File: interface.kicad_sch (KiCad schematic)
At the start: 12 parts, among them IC107 RC4558, IC501 D91317GD, IC502 MSM5205, IC503 4053, IC504 4053

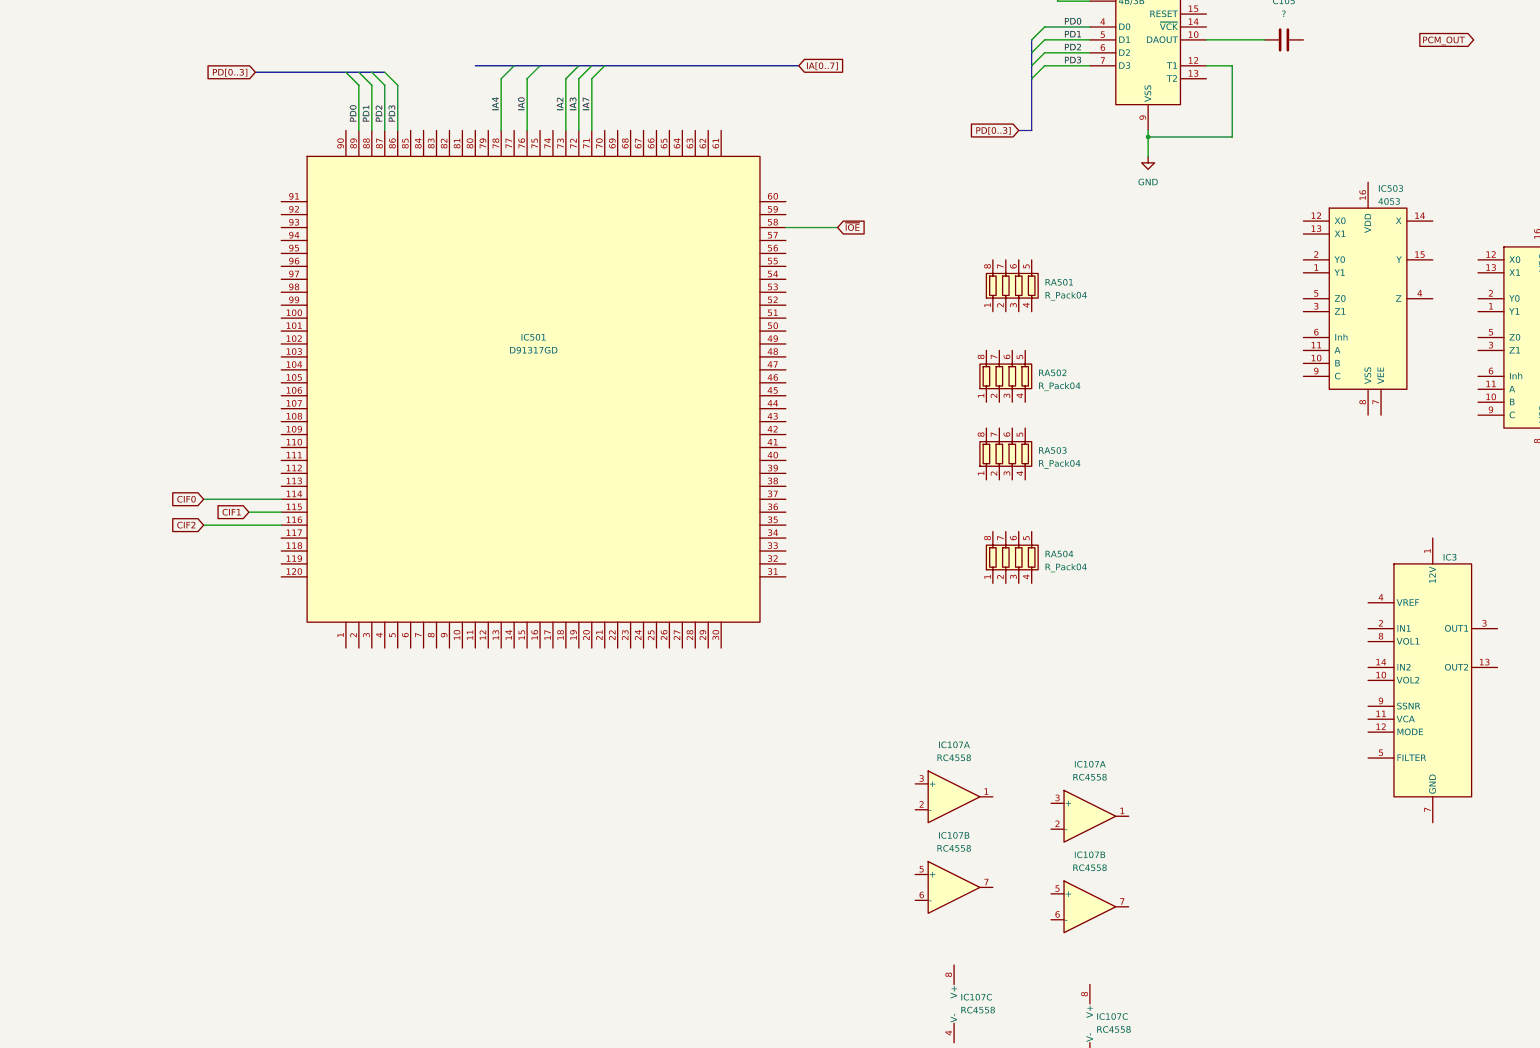
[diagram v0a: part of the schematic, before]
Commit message: Add proper scans, redo traces.
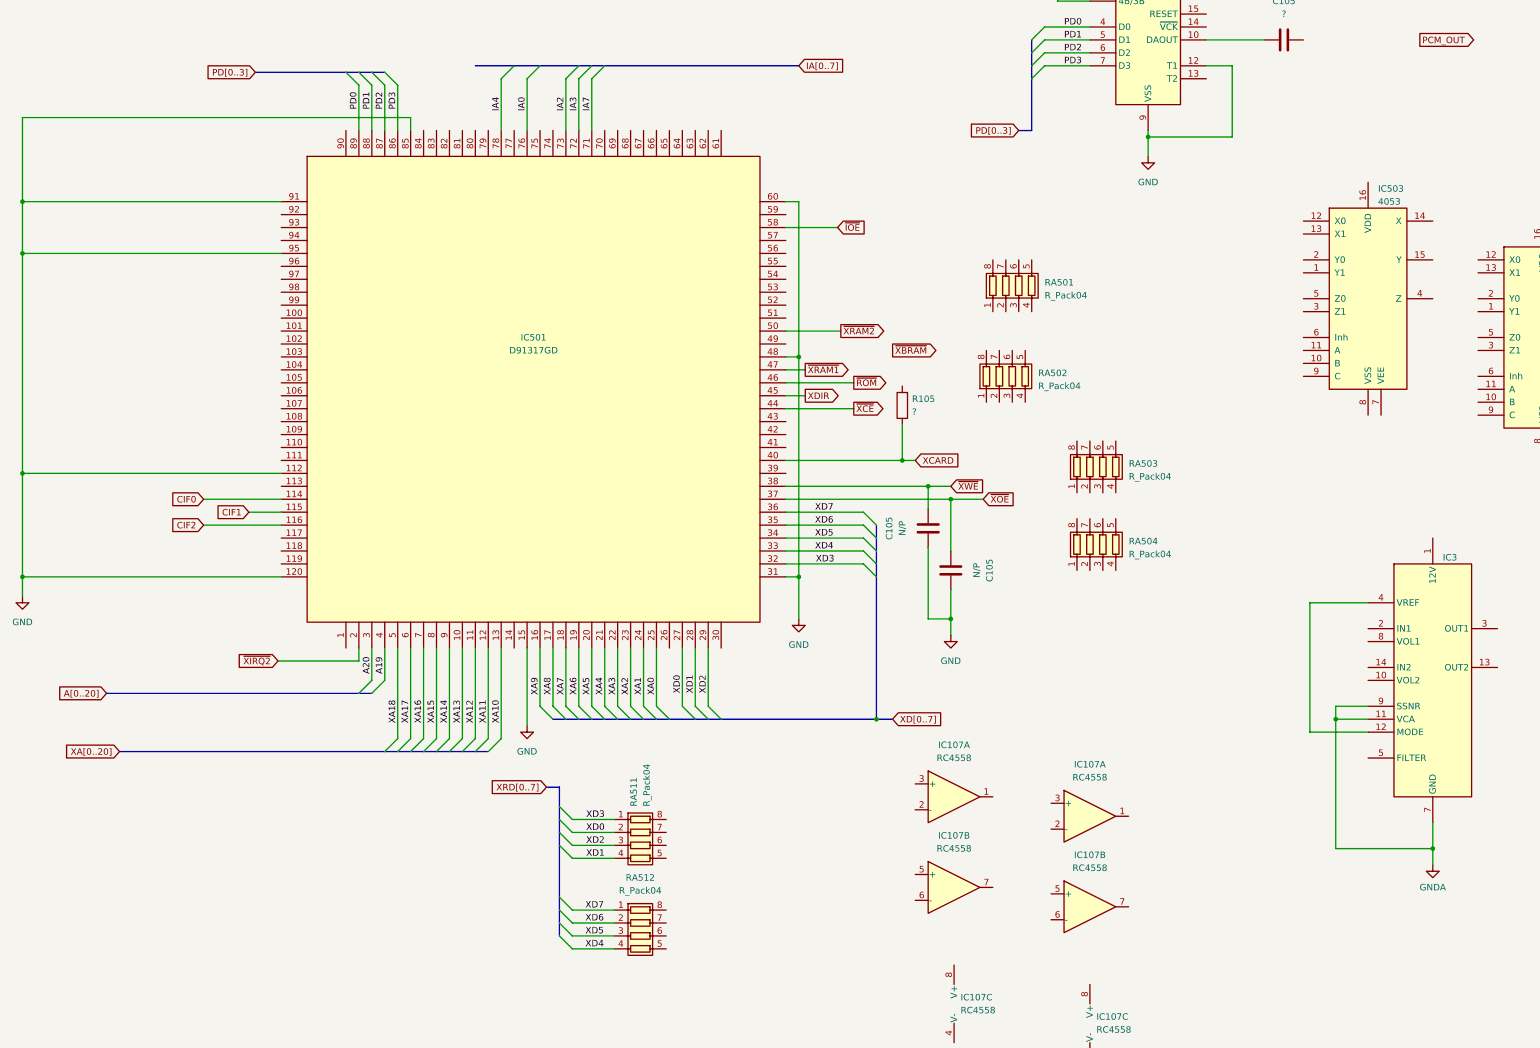
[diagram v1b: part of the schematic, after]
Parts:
- added C105 (x2): N/P, Capacitor_SMD:C_0805_2012Metric, symbol Device:C
- added R105: ?, Resistor_SMD:R_0805_2012Metric, symbol Device:R
- added RA511, RA512: R_Pack04, Resistor_SMD:R_Array_Concave_4x0603, symbol Device:R_Pack04
- IC3: footprint Connector_PinHeader_2.54mm:PinHeader_2x07_P2.54mm_Vertical -> A-PCENGINE:ZIP-14
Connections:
- net GND: now also IC501.112, IC501.120, IC501.15, IC501.31, IC501.48, IC501.60, IC501.85, IC501.91, IC501.95, C105.1, C105.1
- net XA13: now reaches IC501.10
- net XA12: now reaches IC501.11
- net XA11: now reaches IC501.12
- net XA10: now reaches IC501.13
- net XA9: now reaches IC501.16
- net XA8: now reaches IC501.17
- net XA7: now reaches IC501.18
- net XA6: now reaches IC501.19
- net ~{XIRQ2}: now reaches IC501.2
- net XA5: now reaches IC501.20
- net XA4: now reaches IC501.21
- net XA3: now reaches IC501.22
- net XA2: now reaches IC501.23
- net XA1: now reaches IC501.24
- net XA0: now reaches IC501.25
- net XD0: now reaches IC501.27
- net XD0: now also RA511.2 (R2.1)
- net XD1: now reaches IC501.28
- net XD1: now also RA511.4 (R4.1)
- net XD2: now reaches IC501.29
- net XD2: now also RA511.3 (R3.1)
- net A20: now reaches IC501.3
- net XD3: now reaches IC501.32
- net XD3: now also RA511.1 (R1.1)
- net XD4: now reaches IC501.33
- net XD4: now also RA512.4 (R4.1)
- net XD5: now reaches IC501.34
- net XD5: now also RA512.3 (R3.1)
- net XD6: now reaches IC501.35
- net XD6: now also RA512.2 (R2.1)
- net XD7: now reaches IC501.36
- net XD7: now also RA512.1 (R1.1)
- net ~{XOE}: now reaches IC501.37
- net ~{XOE}: now also C105.2
- net ~{XWE}: now reaches IC501.38
- net ~{XWE}: now also C105.2
- net A19: now reaches IC501.4
- net XCARD: now reaches IC501.40
- net XCARD: now also R105.1
- net ~{XCE}: now reaches IC501.44
- net XDIR: now reaches IC501.45
- net ~{ROM}: now reaches IC501.46
- net ~{XRAM1}: now reaches IC501.47
- net XA18: now reaches IC501.5
- net ~{XRAM2}: now reaches IC501.50
- net XA17: now reaches IC501.6
- net XA16: now reaches IC501.7
- net XA15: now reaches IC501.8
- net XA14: now reaches IC501.9
- net GNDA: now reaches IC3.11 (VCA)
- net GNDA: now also IC3.7 (GND), IC3.9 (SSNR)
- net at IC3.12 (MODE): now also IC3.4 (VREF)
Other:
- moved on the sheet: RA503, RA504

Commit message: More tracing.
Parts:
- added RA513: R_Pack04, Resistor_SMD:R_Array_Concave_4x0603, symbol Device:R_Pack04
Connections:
- net CIF1: now also IC501.119; no longer IC501.115
- net IA0: now also IC501.73; no longer IC501.76
- net IA2: now also IC501.71; no longer IC501.73
- net IA3: now also IC501.70; no longer IC501.72
- net IA4: now also IC501.69; no longer IC501.78
- net IA7: now also IC501.66; no longer IC501.71
- net ~{IOE}: no longer IC501.58
- net CFX1: now reaches IC501.117
- net CFX0: now reaches IC501.118
- net ID3: now reaches IC501.56
- net ID3: now also RA513.4 (R4.1)
- net ID2: now reaches IC501.57
- net ID2: now also RA513.3 (R3.1)
- net ID0: now reaches IC501.59
- net ID0: now also RA513.1 (R1.1)
- net ~{IOE1}: now reaches IC501.62
- net ~{IW1}: now reaches IC501.63
- net ~{IOE0}: now reaches IC501.64
- net ~{IW0}: now reaches IC501.65
- net IA6: now reaches IC501.67
- net IA5: now reaches IC501.68
- net ~{IRAS}: now reaches IC501.77
- new net CFX2: IC501.115
- new net IA1: IC501.72
- new net ID1: IC501.58, RA513.2 (R2.1)
- new net ~{ICAS}: IC501.76

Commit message: Yet more tracing.
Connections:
- net CFX0: now also RA502.2 (R2.1)
- net CFX1: now also RA501.3 (R3.1)
- net CIF0: now also RA501.4 (R4.1)
- net CIF1: now also RA502.1 (R1.1)
- net CIF2: now also RA501.2 (R2.1)
- net GND: now also IC502.2 (S2)
- net CFX3: now reaches RA504.1 (R1.1)
- net CFX3: now also IC501.103
- net CFX4: now reaches RA504.2 (R2.1)
- net CFX4: now also IC501.102
- net CFX5: now reaches RA504.3 (R3.1)
- net CFX5: now also IC501.101
- net CFX6: now reaches RA504.4 (R4.1)
- net CFX6: now also IC501.100
- net at RA504.5 (R4.2): now also RA503.5 (R4.2), RA503.6 (R3.2), RA503.7 (R2.2), RA503.8 (R1.2), RA504.6 (R3.2), RA504.7 (R2.2), RA504.8 (R1.2)
- net EXCK: now reaches IC501.105
- net EXCK: now also RA502.4 (R4.1)
- net CIF4: now reaches IC501.107
- net CIF3: now reaches IC501.108
- net CIF3: now also IC501.113, RA501.1 (R1.1)
- net ~{VCK}: now reaches IC501.82
- net ~{VCK}: now also IC502.14 (~{VCK})
- net ~{P_RESET}: now reaches IC501.92
- net ~{P_RESET}: now also IC502.15 (RESET)
- net XT: now reaches IC501.93
- net XT: now also IC502.16 (XT)
- net CFX10: now reaches IC501.96
- net CFX10: now also RA503.4 (R4.1)
- net CFX9: now reaches IC501.97
- net CFX9: now also RA503.3 (R3.1)
- net CFX8: now reaches IC501.98
- net CFX8: now also RA503.2 (R2.1)
- net CFX7: now reaches IC501.99
- net CFX7: now also RA503.1 (R1.1)
- net CFXR2: now reaches RA502.3 (R3.1)
- net at RA502.5 (R4.2): now also RA502.6 (R3.2), RA502.7 (R2.2), RA502.8 (R1.2)
- net at RA501.5 (R4.2): now also RA501.6 (R3.2), RA501.7 (R2.2), RA501.8 (R1.2)
- no-connect marks 0 -> 2
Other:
- moved on the sheet: RA501, RA502, RA503, RA504

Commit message: Power rails, etc.
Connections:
- net GND: now also IC501.39
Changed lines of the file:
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@@
   (junction (at 220.345 180.975) (diameter 0) (color 0 0 0 0)
+  )
+  (junction (at 190.5 152.4) (diameter 0) (color 0 0 0 0)
   )
   (junction (at 82.55 26.67) (diameter 0) (color 0 0 0 0)
@@
     (stroke (width 0) (type default))
   )
-  (wire (pts (xy 190.5 129.54) (xy 190.5 172.72))
+  (wire (pts (xy 190.5 129.54) (xy 190.5 152.4))
     (stroke (width 0) (type default))
   )
@@
     (stroke (width 0) (type default))
   )
+  (wire (pts (xy 190.5 152.4) (xy 190.5 172.72))
+    (stroke (width 0) (type default))
+  )
   (wire (pts (xy 204.47 104.14) (xy 187.96 104.14))
     (stroke (width 0) (type default))
@@
     (stroke (width 0) (type default))
   )
+  (wire (pts (xy 187.96 152.4) (xy 190.5 152.4))
+    (stroke (width 0) (type default))
+  )

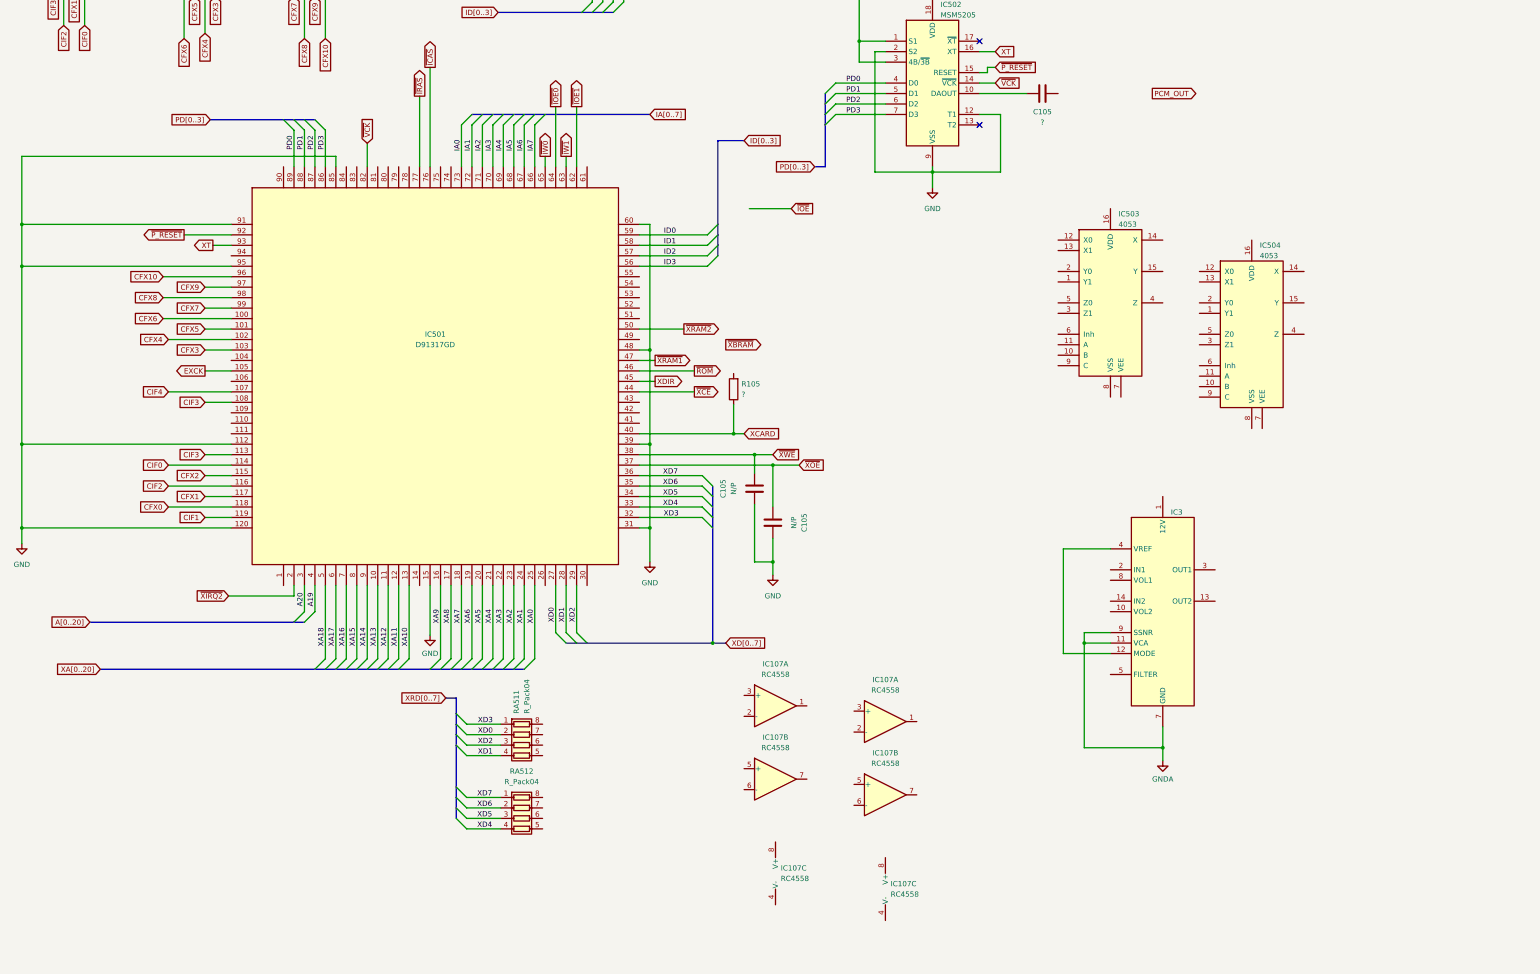
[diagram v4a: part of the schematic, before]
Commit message: IC routing mostly complete, start adding passives.
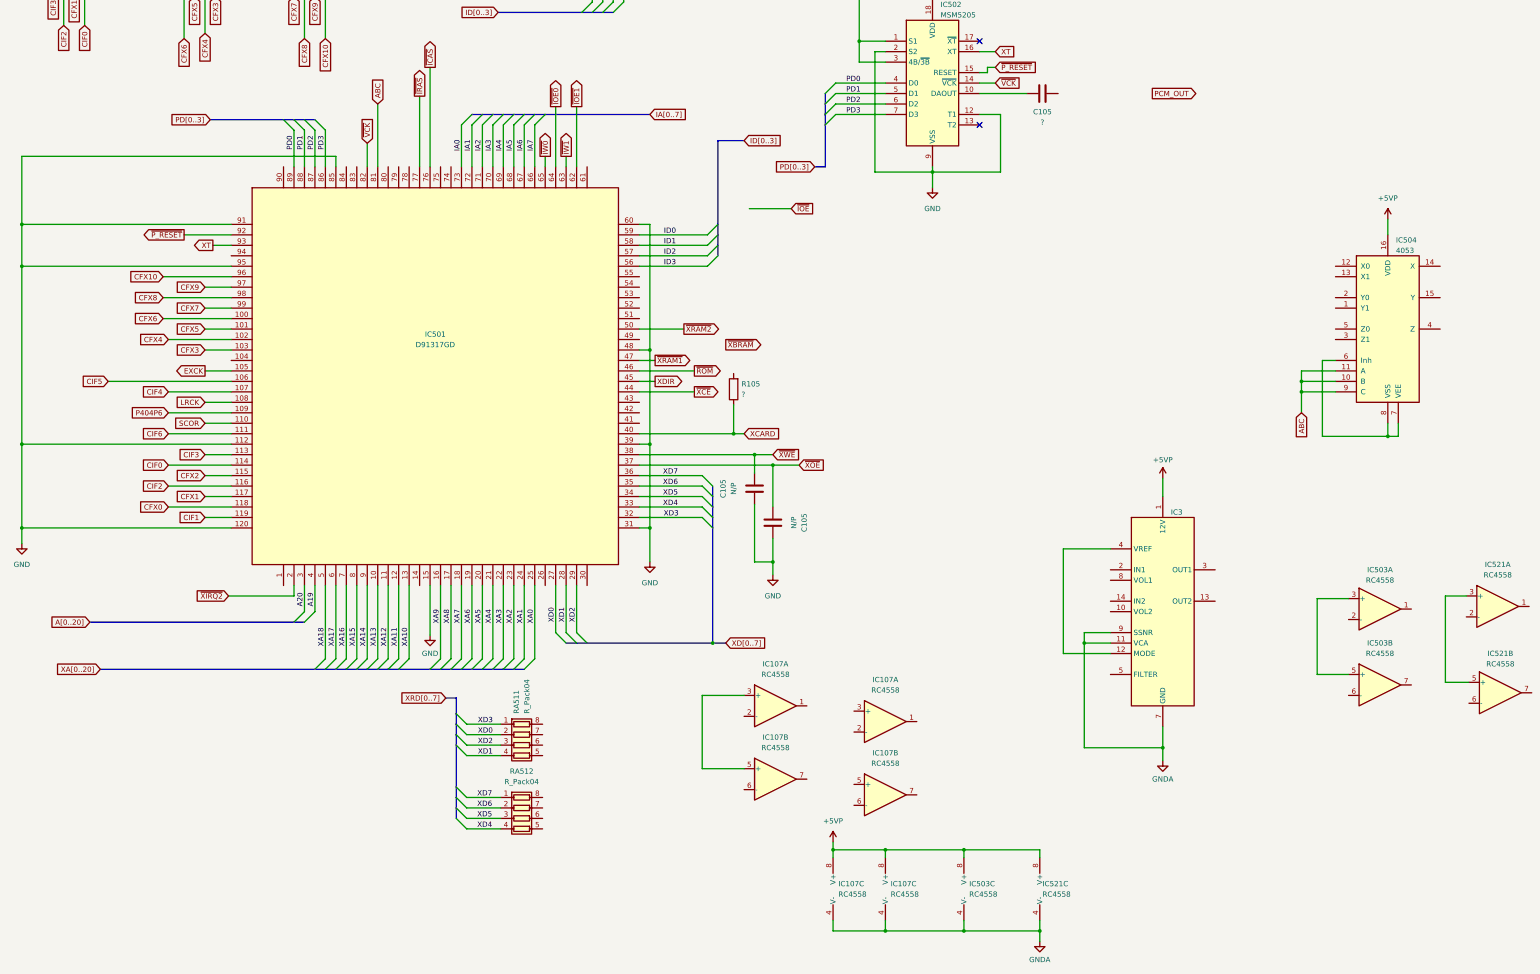
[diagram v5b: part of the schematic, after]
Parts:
- removed IC503: 4053, Package_SO:SOIC-16_4.55x10.3mm_P1.27mm, symbol 4xxx:4053
- added IC503, IC521: RC4558, Package_SO:SO-8_5.3x6.2mm_P1.27mm, symbol Amplifier_Operational:RC4558
- C105: footprint Capacitor_SMD:C_0805_2012Metric -> A-PCENGINE:SMD_0805_Narrow
- R105: footprint Resistor_SMD:R_0805_2012Metric -> A-PCENGINE:SMD_0805_Narrow
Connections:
- net CIF3: no longer IC501.108
- net GNDA: now also IC107.4 (V-), IC107.4 (V-), IC503.4 (V-), IC521.4 (V-)
- net CIF5: now reaches IC501.106
- net P404P6: now reaches IC501.109
- net SCOR: now reaches IC501.110
- net CIF6: now reaches IC501.111
- net ABC: now reaches IC501.81
- net ABC: now also IC504.10 (B), IC504.11 (A), IC504.9 (C)
- net +5VP: now reaches IC107.8 (V+)
- net +5VP: now also IC107.8 (V+), IC3.1 (12V), IC504.16 (VDD), IC503.8 (V+), IC521.8 (V+)
- net at IC107.5 (+): now also IC107.3 (+)
- net at IC504.6 (Inh): now also IC504.7 (VEE), IC504.8 (VSS)
- new net: IC503.3 (+), IC503.5 (+)
- new net: IC521.3 (+), IC521.5 (+)
- new net LRCK: IC501.108
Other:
- moved on the sheet: IC107C, IC504

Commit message: Bunch of passives and what-not.
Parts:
- added L106: ~, A-PCENGINE:SMD_0805_Narrow, symbol Device:L
- R105: footprint A-PCENGINE:SMD_0805_Narrow -> A-PCENGINE:SMD_0805_Narrow_Long
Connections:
- net GND: now also IC501.75, RA503.5 (R4.2), RA503.6 (R3.2), RA503.7 (R2.2), RA503.8 (R1.2), RA504.5 (R4.2), RA504.6 (R3.2), RA504.7 (R2.2), RA504.8 (R1.2)
- net +5V: now reaches RA511.5 (R4.2)
- net +5V: now also R105.2, RA511.6 (R3.2), RA511.7 (R2.2), RA511.8 (R1.2), RA512.5 (R4.2), RA512.6 (R3.2), RA512.7 (R2.2), RA512.8 (R1.2), RA513.5 (R4.2), RA513.6 (R3.2), RA513.7 (R2.2), RA513.8 (R1.2), L106.2
- net at IC501.1: now also IC501.14, IC501.26, IC501.30, IC501.61, IC501.90, L106.1
- net +5VD: now reaches RA502.5 (R4.2), RA502.6 (R3.2), RA502.7 (R2.2), RA502.8 (R1.2)
- net +5VD: now also RA501.5 (R4.2), RA501.6 (R3.2), RA501.7 (R2.2), RA501.8 (R1.2)
- no-connect marks 2 -> 10
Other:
- moved on the sheet: RA502, RA503, RA504, RA511, RA512, RA513
